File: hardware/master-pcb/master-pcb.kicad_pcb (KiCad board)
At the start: 4 copper layers, 77.5 x 65.5 mm, 56 parts, among them J1 RS-485 OUT, J2 INT IN 0-8, J4 UNDERGLOW OUT, SW1 PLAYER_ID, U1 Teensy 4.0, U2 THVD1429, U3 SN74AHCT125

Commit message: Harness rework: INT twisted pair on JST XH, RS-485 shield on Micro-Fit pin 3
Two cabling changes, both of which replace earlier decisions.

INT goes twisted pair (signal + dedicated GND return)
-----------------------------------------------------
The panel side needed no change: J9 pin 2 was provisioned as GND for
exactly this on 2026-07-24. On the master, the 9-position pluggable
Euroblock is replaced by nine JST XH 2-pin vertical headers (B2B-XH-A),
placed as J2, J3, J5-J11 -- non-contiguous because renumbering J4 would
churn the docs for no gain.

Nine discrete 5.08mm screw blocks were rejected outright: ~92mm of board
edge against a 77.5mm board. XH is top-entry, so it needs no board edge
at all and the nine fit in roughly what the Euroblock vacated (~42x13.5
vs 45.72x12.0mm). XH is also keyed, so signal and GND cannot be swapped
at assembly -- that swap on a screw terminal ties INT to GND and reads as
a permanently stuck press. Keeping XH here while panel FSRs stay PH also
means an FSR lead cannot be plugged into an INT header.

Cost accepted: nine plugs instead of one detachable block.

Connectors are silkscreened by panel position (UL/U/UR/L/C/R/DL/D/DR),
left to right in panel order 0->8. This supersedes the old "J2 position 1
is panel 8" reversal note -- the mapping is now monotonic.

RS-485 shield terminated on pin 3
---------------------------------
Reverses the 2026-07-24 "drain floating at both ends" decision. That
reasoning was sound on its own terms; this takes the upgrade path the
old note itself described as a five-minute change.

Hybrid grounding, one continuous shield master -> panel 8:
  - master J1 pin 3 -> GND, the single DC reference for the network
  - each panel: RS485_Shield passes J8.3 -> J10.3, no local GND tie,
    plus C57 100nF || R20 1M to GND near J8

The per-panel caps are not decoration: ~6-8m of foil grounded at one end
only resonates near 10MHz, inside 1Mbps harmonic content. The cap grounds
it at RF while blocking DC, so no loo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
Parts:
- added J10: B2B-XH-A, Connector_JST:JST_XH_B2B-XH-A_1x02_P2.50mm_Vertical, F.Cu at (105.3, 85.5)
- added J11: B2B-XH-A, Connector_JST:JST_XH_B2B-XH-A_1x02_P2.50mm_Vertical, F.Cu at (98.3, 85.5)
- added J3: B2B-XH-A, Connector_JST:JST_XH_B2B-XH-A_1x02_P2.50mm_Vertical, F.Cu at (147.3, 85.5)
- added J5: B2B-XH-A, Connector_JST:JST_XH_B2B-XH-A_1x02_P2.50mm_Vertical, F.Cu at (140.3, 85.5)
- added J6: B2B-XH-A, Connector_JST:JST_XH_B2B-XH-A_1x02_P2.50mm_Vertical, F.Cu at (133.3, 85.5)
- added J7: B2B-XH-A, Connector_JST:JST_XH_B2B-XH-A_1x02_P2.50mm_Vertical, F.Cu at (126.3, 85.5)
- added J8: B2B-XH-A, Connector_JST:JST_XH_B2B-XH-A_1x02_P2.50mm_Vertical, F.Cu at (119.3, 85.5)
- added J9: B2B-XH-A, Connector_JST:JST_XH_B2B-XH-A_1x02_P2.50mm_Vertical, F.Cu at (112.4, 85.5)
- J2: value INT IN 0-8 -> B2B-XH-A; footprint master-pcb:TerminalBlock_Molex_39531_1x09_P5.08mm_Vertical -> Connector_JST:JST_XH_B2B-XH-A_1x02_P2.50mm_Vertical
- moved R6 12.4 mm to (154.4, 90.5)
- moved U3 11.9 mm to (156.4, 98.4), turned to -90 degrees
- moved D2 10.9 mm to (154.4, 91.2)
- moved R7 10.8 mm to (147.3, 90.5)
- moved J2 10.7 mm to (154.4, 85.5), turned to 90 degrees
- moved H1 10.4 mm to (163.1, 88.8)
- moved R8 9.28 mm to (140.3, 90.5)
- moved D3 9.03 mm to (147.3, 91.2)
- moved R14 8.27 mm to (98.3, 90.5)
- moved R9 8.05 mm to (133.3, 90.5)
- moved D4 7.26 mm to (140.3, 91.2)
- moved R13 7.25 mm to (105.3, 90.5)
- moved C2 7.23 mm to (155.2, 108.3), turned to 180 degrees
- moved R10 7.09 mm to (126.3, 90.5)
- moved R12 6.67 mm to (112.4, 90.5)
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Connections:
- J1 pad 3: unconnected-(J1-Pin_3-Pad3) -> GND
- J2 pad 2: Net-(D3-K) -> GND
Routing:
- net GND: track 46.3 -> 2.44 mm, vias 201 -> 481
- net INT_DR: track 22.3 -> 38.4 mm
- net INT_D: track 19.7 -> 33.9 mm
- net INT_DL: track 17.3 -> 29.3 mm
- net INT_UL: track 13.7 -> 23.5 mm
- net INT_R: track 14.7 -> 24.3 mm
- net Net-(R3-Pad1): track 29.7 -> 38.1 mm
- net INT_C: track 12.3 -> 20.4 mm
- net INT_U: track 11.8 -> 19.6 mm
- net INT_UR: track 10.7 -> 17.8 mm
- net +5VDC_USB: track 63.4 -> 70.5 mm
- net INT_L: track 11.1 -> 18.2 mm
- net UNDERGLOW_DATA: track 47.2 -> 53.1 mm
- net Net-(D3-K): track 12.5 -> 7.39 mm
- net Net-(D2-K): track 12.5 -> 7.39 mm
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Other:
- outline, holes or cut-outs redrawn
- board text added: "C"
- board text added: "D"
- board text added: "DL"
- board text added: "DR"
- board text added: "L"
- board text added: "R"
- board text added: "SH"
- board text added: "U"
- board text added: "UL"
- board text added: "UR"
- board text removed: "DR D DL R C L UR U UL"
- board text removed: "NC"

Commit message: silkscreen: fix FSR East/RS-485 typos, drop fab placeholder, add year
Found while building the external-review image package:

- panel: J4 on the right edge was silkscreened "FSR West", same as J7 on
  the left. It is FSR East.
- panel: the two bus test points read "RS-495 A/B" -> RS-485.
- panel + master: removed the fab order-number placeholder text.
- all boards: appended the year to the name/rev block, which the review
  conventions ask for alongside board name and revision.
- master: moved 5 graphics from F.Mask to F.Silkscreen.

dual-panel's silkscreen carries the same year/placeholder edits but that
file also has unrelated changes, so it is committed separately.
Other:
- board text added: "Kraken Pad by SenPi MCU : Rev 1.0 : 2026"
- board text removed: "Kraken Pad by SenPi MCU : Rev 1.0"
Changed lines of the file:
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@@
 		)
 		(fill yes)
-		(layer "F.Mask")
+		(layer "F.SilkS")
 	)
 	(gr_poly
@@
 		)
 		(fill yes)
-		(layer "F.Mask")
+		(layer "F.SilkS")
 	)
 	(gr_poly
@@
 		)
 		(fill yes)
-		(layer "F.Mask")
+		(layer "F.SilkS")
 	)
 	(gr_poly
@@
 		)
 		(fill yes)
-		(layer "F.Mask")
+		(layer "F.SilkS")
 	)
 	(gr_poly
@@
 		)
 		(fill yes)
-		(layer "F.Mask")
+		(layer "F.SilkS")
 	)
 	(gr_arc
@@
 		)
 	)
-	(gr_text "Kraken Pad by SenPi\nMCU : Rev 1.0"
-		(at 165.4 106.2 90)
+	(gr_text "Kraken Pad by SenPi\nMCU : Rev 1.0 : 2026"
+		(at 166.1 105.1 90)
 		(layer "F.SilkS")
 		(effects
@@
 	)
 	(segment
+		(start 140.35 85.4)
+		(end 140.35 89.4875)
+		(width 0.2)
+		(layer "F.Cu")
+		(net "Net-(D4-K)")
+	)
+	(segment
+		(start 140.35 88.7)
+		(end 140.35 85.4)
+		(width 0.2)
+		(layer "B.Cu")
+		(net "Net-(D4-K)")
+	)
+	(segment
 		(start 122.2 137.8)
 		(end 120.2 139.8)
@@
 	)
 	(segment
+		(start 119.35 85.4)
+		(end 119.35 89.4875)
+		(width 0.2)
+		(layer "F.Cu")
+		(net "Net-(D7-K)")
+	)
+	(segment
+		(start 119.35 88.7)
+		(end 119.35 85.4)
+		(width 0.2)
+		(layer "B.Cu")
+		(net "Net-(D7-K)")
+	)
+	(segment
 		(start 112.375 85.45)
 		(end 112.375 89.5375)
@@
 	)
 	(segment
+		(start 147.35 89.4875)
+		(end 147.35 85.4)
+		(width 0.2)
+		(layer "F.Cu")
+		(net "Net-(D3-K)")
+	)
+	(segment
+		(start 147.35 88.7)
+		(end 147.35 85.4)
+		(width 0.2)
+		(layer "B.Cu")
+		(net "Net-(D3-K)")
+	)
+	(segment
 		(start 134.2 111.8)
 		(end 108.3 111.8)
@@
 	)
 	(segment
-		(start 147.35 89.4875)
-		(end 147.35 85.4)
-		(width 0.2)
-		(layer "F.Cu")
-		(net "Net-(D3-K)")
-	)
-	(segment
-		(start 147.35 88.7)
-		(end 147.35 85.4)
-		(width 0.2)
-		(layer "B.Cu")
-		(net "Net-(D3-K)")
-	)
-	(segment
-		(start 140.35 85.4)
-		(end 140.35 89.4875)
-		(width 0.2)
-		(layer "F.Cu")
-		(net "Net-(D4-K)")
-	)
-	(segment
-		(start 140.35 88.7)
-		(end 140.35 85.4)
-		(width 0.2)
-		(layer "B.Cu")
-		(net "Net-(D4-K)")
-	)
-	(segment
-		(start 119.35 85.4)
-		(end 119.35 89.4875)
-		(width 0.2)
-		(layer "F.Cu")
-		(net "Net-(D7-K)")
-	)
-	(segment
-		(start 119.35 88.7)
-		(end 119.35 85.4)
-		(width 0.2)
-		(layer "B.Cu")
-		(net "Net-(D7-K)")
-	)
-	(segment
-		(start 98.275 85.45)
-		(end 98.275 89.5375)
-		(width 0.2)
-		(layer "F.Cu")
-		(net "Net-(D10-K)")
-	)
-	(segment
-		(start 98.275 88.75)
-		(end 98.275 85.45)
-		(width 0.2)
-		(layer "B.Cu")
-		(net "Net-(D10-K)")
-	)
-	(segment
 		(start 124.8 127.865)
 		(end 125.475 127.865)
@@
 	)
 	(segment
+		(start 98.275 85.45)
+		(end 98.275 89.5375)
+		(width 0.2)
+		(layer "F.Cu")
+		(net "Net-(D10-K)")
+	)
+	(segment
+		(start 98.275 88.75)
+		(end 98.275 85.45)
+		(width 0.2)
+		(layer "B.Cu")
+		(net "Net-(D10-K)")
+	)
+	(segment

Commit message: master: renumber reference designators contiguously from 1
The review conventions ask that each RefDes type start at 1 with no
numeric gaps. This board was missing D1 and R2. Reannotated, then pushed
through to the layout.

DRC 0, unconnected 0, schematic parity 0, ERC 0 with zones refilled.
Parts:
- renumbered C4 to C10, C3 to C11, C11 to C3, C10 to C4, C9 to C5, C8 to C6, C6 to C8, C5 to C9, D10 to D1, D9 to D2, D8 to D3, D7 to D4, D6 to D5, D5 to D6, D4 to D7, D3 to D8, D2 to D9, H3 to H2, H2 to H3, J4 to J2, J2 to J3, J3 to J4, R4 to R1, R9 to R11, R8 to R12, R7 to R13, R6 to R14, R5 to R2, R1 to R3, R15 to R4, R3 to R5, R14 to R6, R13 to R7, R12 to R8, R11 to R9, TP9 to TP1, TP8 to TP10, TP3 to TP2, TP10 to TP3, TP5 to TP4, TP6 to TP5, TP4 to TP6, TP1 to TP7, TP2 to TP8, TP7 to TP9, U2 to U1, U1 to U2

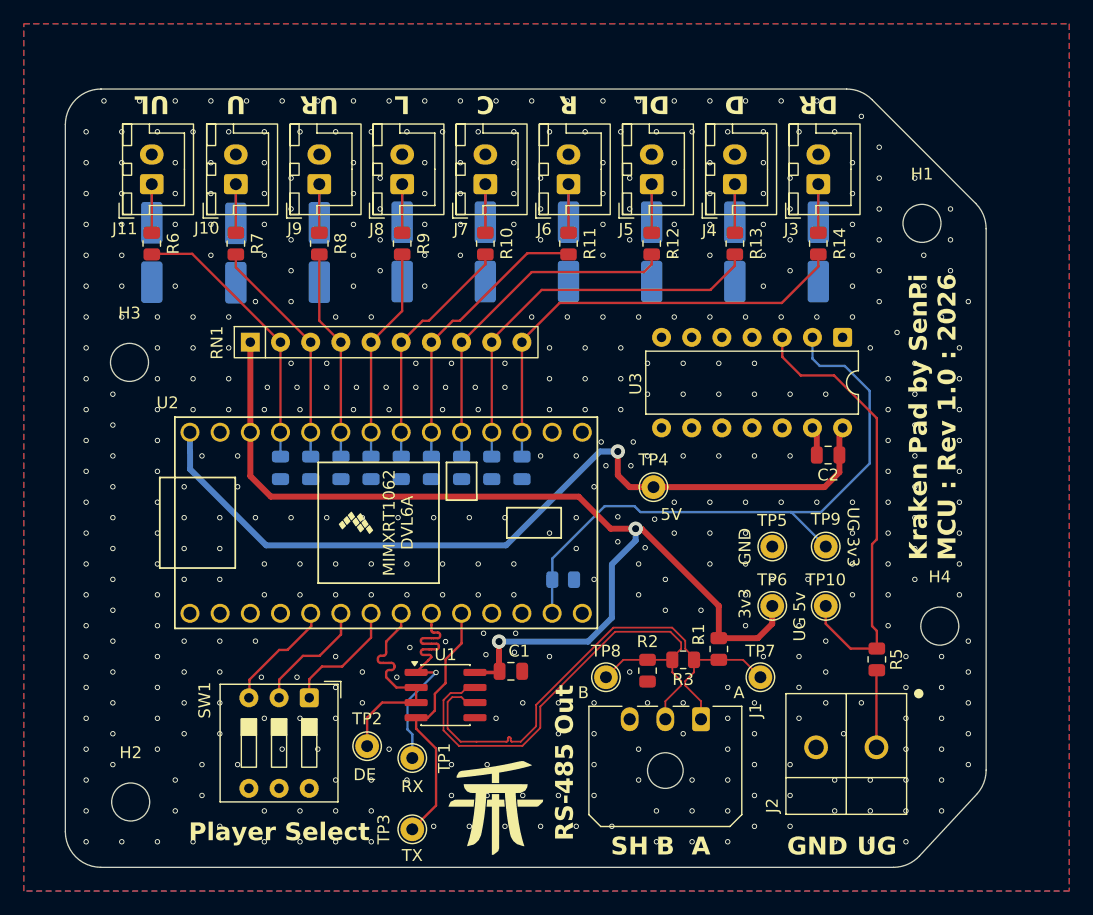
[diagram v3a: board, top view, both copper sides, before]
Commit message: shifter: swap quad SN74AHCT125 for single-gate SN74AHCT1G125 on all boards
External review suggested 74LVC1G34/74LVC1G17 since only one gate was used;
LVC was rejected on input thresholds (VIH = 0.7*VCC = 3.5V at 5V; the 1G17's
Schmitt VT+ max hits 3.33V at 5.5V) but the single-gate idea was right.
SN74AHCT1G125DBVR keeps AHCT's guaranteed TTL VIH of 2.0V in a SOT-23-5:
LCSC C7484, DigiKey 296-4708-1-ND. OE tied to GND; decoupling caps kept.

- panel-pcb U4, dual-panel brain U301, master-pcb U3: schematic symbol,
  footprint, placement and routing redone; spare-gate GND ties and
  no-connects removed
- panel: +5V feed re-routed with a short B.Cu hop under the LED_DATA riser
- master: DIP-14 replaced by SMD; new via drops the B.Cu underglow trace
  onto the A pad, new GND via feeds the OE pad's thermal spokes
- docs + BOMs updated (CLAUDE.md, PANEL_PCB, MASTER_PCB, BOM, UNDERGLOW,
  PRE_ORDER_CHECKLIST, dual-panel README, master-pcb-BOM.csv)

Verification: ERC 0 on all three projects; DRC 0 on panel and master;
dual-panel at its expected floor (19 cross-gap airwires, 90 pre-existing
PWR_FLAG parity conflicts, down from 92).
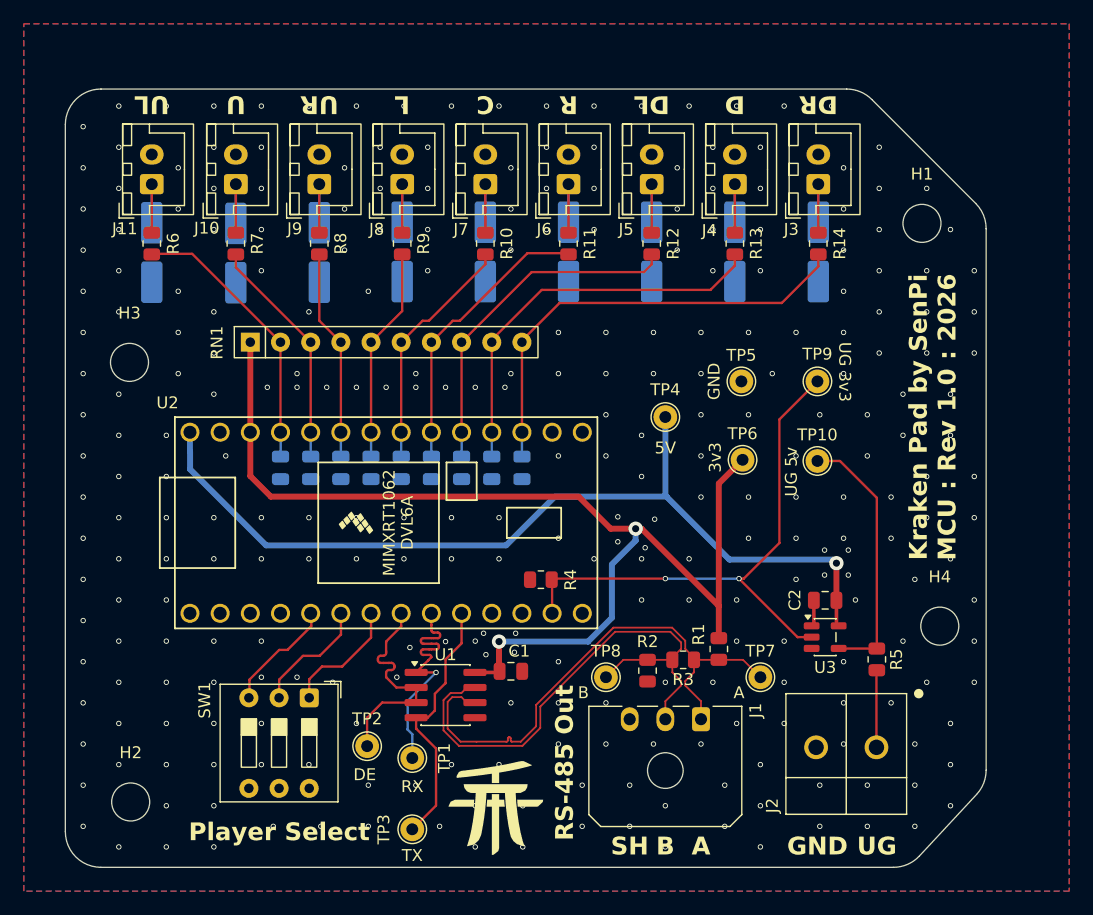
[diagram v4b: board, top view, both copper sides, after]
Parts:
- R4: moved to F.Cu
- U3: value SN74AHCT125 -> SN74AHCT1G125; footprint Package_DIP:DIP-14_W7.62mm -> Package_TO_SOT_SMD:SOT-23-5
- moved U3 25.3 mm to (154.9, 123.6), turned to 0 degrees
- moved TP5 14.1 mm to (147.9, 102.1)
- moved TP9 13.9 mm to (154.3, 102.1)
- moved TP6 12.6 mm to (148.0, 108.7)
- moved C2 12.2 mm to (154.9, 120.5)
- moved TP10 12.2 mm to (154.3, 108.8)
- moved TP4 5.98 mm to (141.5, 105.1)
- moved R4 1.88 mm to (131.0, 118.8), turned to 180 degrees
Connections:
- U3 pad 3: Net-(R5-Pad1) -> GND
- U3 pad 4: GND -> Net-(R5-Pad1)
- U3 pad 5: GND -> +5VDC_USB
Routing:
- net Net-(R5-Pad1): track 38.1 -> 22.2 mm
- net UNDERGLOW_DATA: track 53.1 -> 46.3 mm, vias 0 -> 2
- net +3.3VDC: track 87.7 -> 94.3 mm
- net +5VDC_USB: track 70.5 -> 76.3 mm
- net GND: track 2.44 -> 2.23 mm, vias 481 -> 294
